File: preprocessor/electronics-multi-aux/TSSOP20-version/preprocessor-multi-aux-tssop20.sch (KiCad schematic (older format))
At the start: 16 parts, among them P1 ST-IN, P2 ST-OUT, P3 TH-IN, P4 TH-OUT, P5 AUX-IN, P6 LIGHT CONTROLLER, P7 AUX2-IN, P8 AUX3-IN, U1 MCP1703T-3302E/CB, U2 LPC812M101JTB16_XSON16

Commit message: Add TSSOP 20 versions
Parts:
- removed R1, R2: 1K, Resistor_SMD:R_0603_1608Metric_Pad1.05x0.95mm_HandSolder, symbol Device:R
- added RN2: R_Pack04, Resistor_SMD:R_Array_Convex_4x0603, symbol Device:R_Pack04
- U2: value LPC812M101JTB16_XSON16 -> LPC812M101JDH20; footprint Package_SON:NXP_XSON-16 -> Package_SO:TSSOP-20_4.4x6.5mm_P0.65mm; symbol MCU_NXP_LPC:LPC812M101JTB16 -> MCU_NXP_LPC:LPC812M101JDH20
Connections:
- wire segments 85 -> 82
- no-connect marks 8 -> 16
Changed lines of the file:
@@
 $EndDescr
 $Comp
-L MCU_NXP_LPC:LPC812M101JTB16 U2
+L MCU_NXP_LPC:LPC812M101JDH20 U2
 U 1 1 58AF9BA8
 P 4850 2550
 F 0 "U2" H 4750 2650 10  0001 C CNN
-F 1 "LPC812M101JTB16_XSON16" H 5550 3100 60  0000 C CNN
-F 2 "Package_SON:NXP_XSON-16" H 4750 2650 60  0001 C CNN
+F 1 "LPC812M101JDH20" H 5550 3200 60  0000 C CNN
+F 2 "Package_SO:TSSOP-20_4.4x6.5mm_P0.65mm" H 4750 2650 60  0001 C CNN
 F 3 "" H 4750 2650 60  0000 C CNN
 	1    4850 2550
@@
 L power:+3V3 #PWR04
 U 1 1 58AFA135
-P 4850 1850
-F 0 "#PWR04" H 4850 1700 50  0001 C CNN
-F 1 "+3V3" H 4850 1990 50  0000 C CNN
-F 2 "" H 4850 1850 50  0000 C CNN
-F 3 "" H 4850 1850 50  0000 C CNN
-	1    4850 1850
+P 4850 1750
+F 0 "#PWR04" H 4850 1600 50  0001 C CNN
+F 1 "+3V3" H 4850 1890 50  0000 C CNN
+F 2 "" H 4850 1750 50  0000 C CNN
+F 3 "" H 4850 1750 50  0000 C CNN
+	1    4850 1750
 	1    0    0    -1
 $EndComp
@@
 Connection ~ 9800 4100
 Wire Wire Line
-	4850 1850 4850 1950
-Wire Wire Line
 	2100 1900 1850 1900
 Wire Wire Line
@@
 	1850 1800 2450 1800
 Wire Wire Line
-	3050 1800 3050 2250
-Wire Wire Line
 	1850 2800 2450 2800
 Wire Wire Line
-	3050 2800 3050 2650
-Wire Wire Line
 	7200 2750 8000 2750
-NoConn ~ 5550 2450
 NoConn ~ 5550 2250
 NoConn ~ 4150 2350
 NoConn ~ 4150 2450
-NoConn ~ 4150 2550
 NoConn ~ 4150 2750
 NoConn ~ 4150 2850
@@
 	2400 1350 2100 1350
 Connection ~ 2100 1350
-Text Label 2650 3750 0    50   ~ 0
+Text Label 2900 3750 2    50   ~ 0
 AUX_IN
-Text Label 2650 2800 0    50   ~ 0
+Text Label 2900 2800 2    50   ~ 0
 TH_IN
-Text Label 2650 1800 0    50   ~ 0
+Text Label 2900 1800 2    50   ~ 0
 ST_IN
 Text Label 7200 2750 0    50   ~ 0
 LIGHT_OUT
-$Comp
-L Device:R R1
-U 1 1 58C77CC2
-P 3300 2250
-F 0 "R1" V 3380 2250 50  0000 C CNN
-F 1 "1K" V 3300 2250 50  0000 C CNN
-F 2 "Resistor_SMD:R_0603_1608Metric_Pad1.05x0.95mm_HandSolder" V 3230 2250 50  0001 C CNN
-F 3 "" H 3300 2250 50  0001 C CNN
-	1    3300 2250
-	0    1    1    0
-$EndComp
-$Comp
-L Device:R R2
-U 1 1 58C77D77
-P 3300 2650
-F 0 "R2" V 3380 2650 50  0000 C CNN
-F 1 "1K" V 3300 2650 50  0000 C CNN
-F 2 "Resistor_SMD:R_0603_1608Metric_Pad1.05x0.95mm_HandSolder" V 3230 2650 50  0001 C CNN
-F 3 "" H 3300 2650 50  0001 C CNN
-	1    3300 2650
-	0    1    1    0
-$EndComp
-Wire Wire Line
-	3050 2250 3150 2250
-Wire Wire Line
-	3050 2650 3150 2650
 $Comp
 L power:PWR_FLAG #FLG013
@@
 	1950 2500 1950 3000
 Wire Wire Line
-	2450 1800 3050 1800
-Wire Wire Line
-	2450 2800 3050 2800
+	2450 1800 2900 1800
+Wire Wire Line
+	2450 2800 2900 2800
 Wire Wire Line
 	2100 1350 2100 1900
@@
 Wire Wire Line
 	1950 4450 1850 4450
-Text Label 2650 4250 0    50   ~ 0
-AUX2_IN
 Connection ~ 2100 3850
 $Comp
@@
 	1950 4950 1850 4950
 Connection ~ 1950 4950
-Text Label 2650 4750 0    50   ~ 0
+Text Label 2900 4750 2    50   ~ 0
 AUX3_IN
 Wire Wire Line
@@
 	8900 4400 8900 4600
 Wire Wire Line
-	4850 3150 4850 3300
-Wire Wire Line
-	3450 2650 4150 2650
-Wire Wire Line
-	6250 2350 5550 2350
-NoConn ~ 5550 2550
-Wire Wire Line
-	5550 2650 5950 2650
-Wire Wire Line
-	3450 2250 4150 2250
-Text Label 6250 2750 2    50   ~ 0
+	4850 3250 4850 3300
+Wire Wire Line
+	3600 2550 4150 2550
+Wire Wire Line
+	6250 2350 5950 2350
+Wire Wire Line
+	3600 2150 4150 2150
+Text Label 6250 2450 2    50   ~ 0
 LIGHT
-Text Label 3600 2250 0    50   ~ 0
+Text Label 3600 2150 0    50   ~ 0
 ST
-Text Label 3600 2650 0    50   ~ 0
+Text Label 3600 2550 0    50   ~ 0
 TH
-Text Label 6250 2850 2    50   ~ 0
+Text Label 6250 2550 2    50   ~ 0
 AUX
+Text Label 3600 2950 0    50   ~ 0
+AUX2
 Text Label 6250 2350 2    50   ~ 0
-AUX2
-Text Label 6250 2650 2    50   ~ 0
 AUX3
 $Comp
@@
 $EndComp
 Wire Wire Line
-	5950 2650 6250 2650
-Connection ~ 5950 2650
-Wire Wire Line
-	5550 2750 6250 2750
-Wire Wire Line
-	5950 2650 5950 2950
-Wire Wire Line
-	5550 2850 6250 2850
-Wire Wire Line
-	3650 3750 3650 4050
-Wire Wire Line
-	3650 4050 4550 4050
-Wire Wire Line
-	1850 3750 3650 3750
-Wire Wire Line
-	3650 4250 3650 4150
-Wire Wire Line
-	3650 4150 4550 4150
-Wire Wire Line
-	1850 4250 3650 4250
-Wire Wire Line
-	3750 4250 3750 4750
-Wire Wire Line
-	1850 4750 3750 4750
-Wire Wire Line
-	3750 4250 4550 4250
+	4000 4050 4550 4050
+Wire Wire Line
+	1850 3750 2900 3750
+Wire Wire Line
+	4000 4150 4550 4150
+Wire Wire Line
+	1850 4750 2900 4750
+Wire Wire Line
+	4000 4250 4550 4250
 Wire Wire Line
 	4550 4350 4000 4350
@@
 Text Label 5500 4250 2    50   ~ 0
 AUX3
+NoConn ~ 4150 2250
+NoConn ~ 4150 2650
+Wire Wire Line
+	4150 2950 3600 2950
+NoConn ~ 5550 2150
+Connection ~ 5950 2350
+Wire Wire Line
+	5950 2350 5550 2350
+Wire Wire Line
+	5950 2350 5950 2950
+Wire Wire Line
+	5550 2450 6250 2450
+Wire Wire Line
+	5550 2550 6250 2550
+NoConn ~ 5550 2650
+NoConn ~ 5550 2750
+NoConn ~ 5550 2950
+NoConn ~ 5550 2850
+$Comp
+L Device:R_Pack04 RN2
+U 1 1 6028CA7F
+P 4750 5000
+F 0 "RN2" V 4333 5000 50  0000 C CNN
+F 1 "R_Pack04" V 4424 5000 50  0000 C CNN
+F 2 "Resistor_SMD:R_Array_Convex_4x0603" V 5025 5000 50  0001 C CNN
+F 3 "~" H 4750 5000 50  0001 C CNN
+	1    4750 5000
+	0    1    1    0
+$EndComp
+Text Label 4000 4050 0    50   ~ 0
+AUX_IN
+Wire Wire Line
+	1850 4250 2900 4250
+Text Label 2900 4250 2    50   ~ 0
+AUX2_IN
+Text Label 4000 4150 0    50   ~ 0
+AUX2_IN
+Text Label 4000 4250 0    50   ~ 0
+AUX3_IN
+Wire Wire Line
+	4000 5000 4550 5000
+Wire Wire Line
+	4000 5100 4550 5100
+NoConn ~ 4550 4900
+NoConn ~ 4550 4800
+NoConn ~ 4950 4900
+NoConn ~ 4950 4800
+Wire Wire Line
+	5500 5000 4950 5000
+Wire Wire Line
+	5500 5100 4950 5100
+Text Label 4000 5000 0    50   ~ 0
+ST_IN
+Text Label 4000 5100 0    50   ~ 0
+TH_IN
+Text Label 5500 5000 2    50   ~ 0
+ST
+Text Label 5500 5100 2    50   ~ 0
+TH
+Wire Wire Line
+	4850 1750 4850 1850
 $EndSCHEMATC

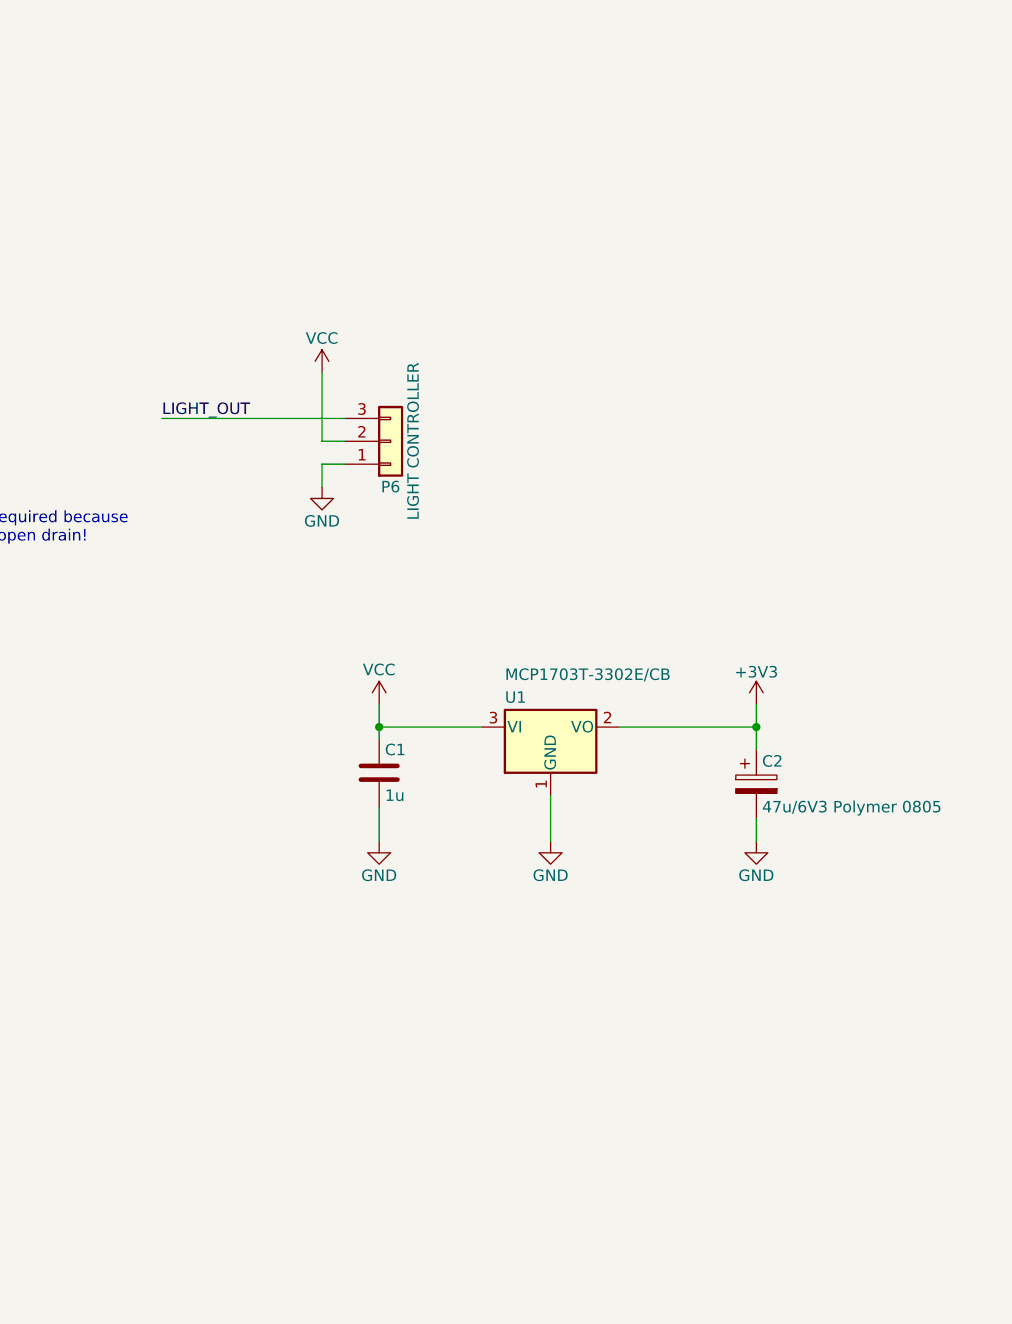
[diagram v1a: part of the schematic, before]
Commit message: Add AUX2 pin assignment info
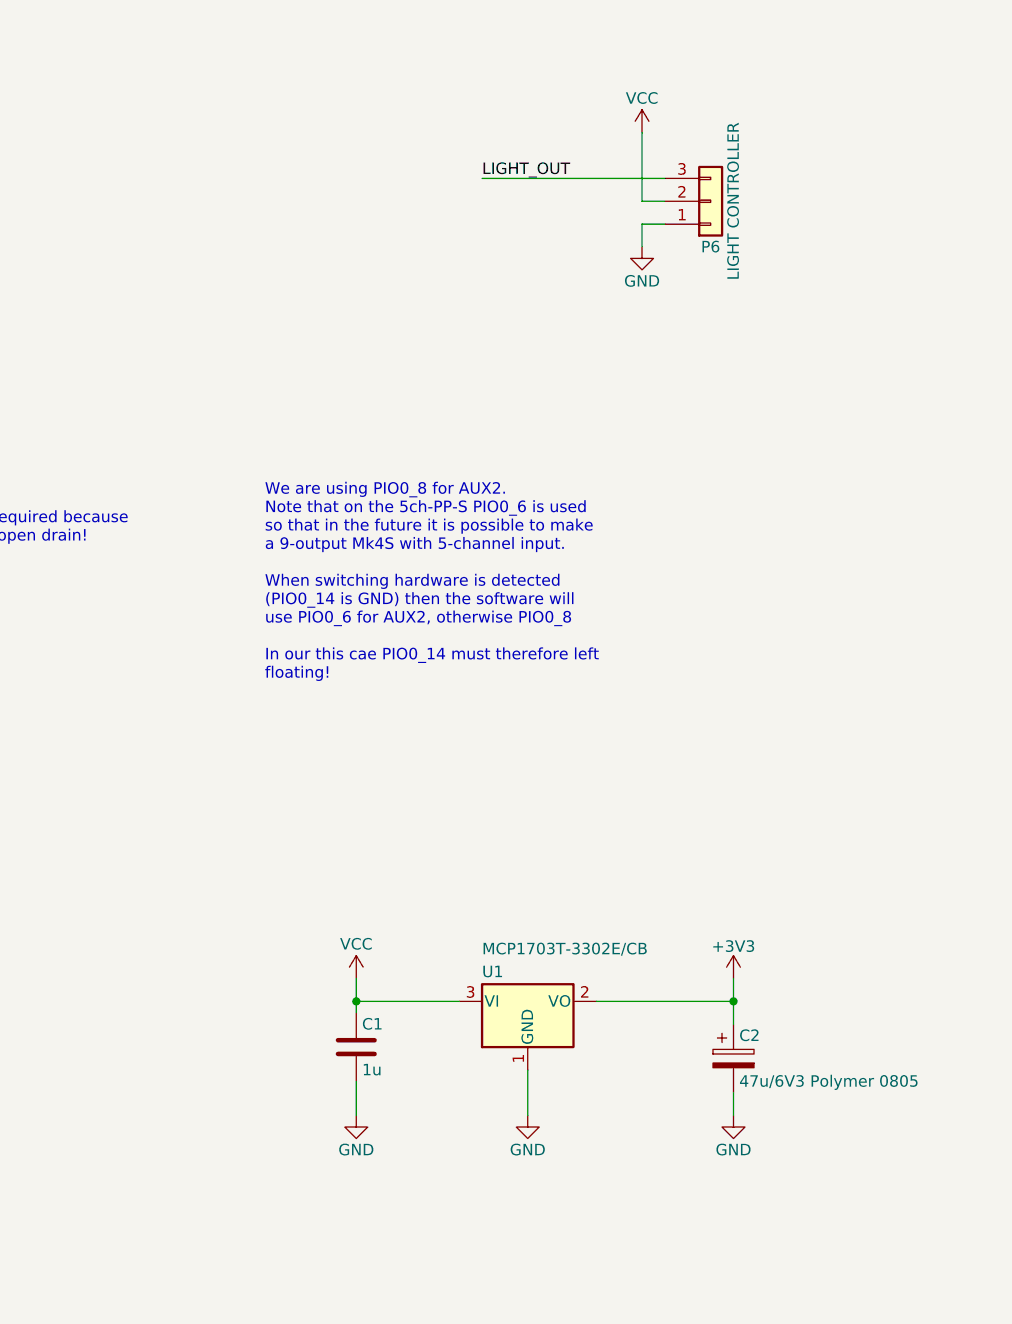
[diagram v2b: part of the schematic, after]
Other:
- note added: "We are using PIO0_8 for AUX2.\nNote that on the 5ch-PP-S PIO0_6 is used\nso that in the future it is possible to make\na 9-output Mk4S with 5-channel input.\n\nWhen switching hardware is detected \n(PIO0_14 is GND) then the software will\nuse PIO0_6 for AUX2, otherwise PIO0_8\n\nIn our this cae PIO0_14 must therefore left \nfloating!"
- moved on the sheet: C1, C2, P6, U1
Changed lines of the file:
@@
 L Regulator_Linear:MCP1703A-3302_SOT23 U1
 U 1 1 58AF9BBC
-P 8900 4100
-F 0 "U1" H 8700 4200 50  0000 L BNN
-F 1 "MCP1703T-3302E/CB" H 8700 4300 50  0000 L BNN
-F 2 "Package_TO_SOT_SMD:SOT-23W" H 9050 3650 30  0001 C CNN
-F 3 "" H 8900 4100 60  0000 C CNN
-	1    8900 4100
+P 8800 5300
+F 0 "U1" H 8600 5400 50  0000 L BNN
+F 1 "MCP1703T-3302E/CB" H 8600 5500 50  0000 L BNN
+F 2 "Package_TO_SOT_SMD:SOT-23W" H 8950 4850 30  0001 C CNN
+F 3 "" H 8800 5300 60  0000 C CNN
+	1    8800 5300
 	1    0    0    -1
 $EndComp
@@
 L Connector_Generic:Conn_01x03 P6
 U 1 1 58AF9DBB
-P 8200 2850
-F 0 "P6" H 8200 3050 50  0000 C CNN
-F 1 "LIGHT CONTROLLER" V 8300 2850 50  0000 C CNN
-F 2 "Connector_PinHeader_2.54mm:PinHeader_1x03_P2.54mm_Vertical" H 8200 2850 50  0001 C CNN
-F 3 "" H 8200 2850 50  0000 C CNN
-	1    8200 2850
+P 9600 1800
+F 0 "P6" H 9600 2000 50  0000 C CNN
+F 1 "LIGHT CONTROLLER" V 9700 1800 50  0000 C CNN
+F 2 "Connector_PinHeader_2.54mm:PinHeader_1x03_P2.54mm_Vertical" H 9600 1800 50  0001 C CNN
+F 3 "" H 9600 1800 50  0000 C CNN
+	1    9600 1800
 	1    0    0    1
 $EndComp
@@
 L power:GND #PWR02
 U 1 1 58AFA0BE
-P 8150 4600
-F 0 "#PWR02" H 8150 4350 50  0001 C CNN
-F 1 "GND" H 8150 4450 50  0000 C CNN
-F 2 "" H 8150 4600 50  0000 C CNN
-F 3 "" H 8150 4600 50  0000 C CNN
-	1    8150 4600
+P 8050 5800
+F 0 "#PWR02" H 8050 5550 50  0001 C CNN
+F 1 "GND" H 8050 5650 50  0000 C CNN
+F 2 "" H 8050 5800 50  0000 C CNN
+F 3 "" H 8050 5800 50  0000 C CNN
+	1    8050 5800
 	1    0    0    -1
 $EndComp
@@
 L power:VCC #PWR06
 U 1 1 58AFA193
-P 8150 4000
-F 0 "#PWR06" H 8150 3850 50  0001 C CNN
-F 1 "VCC" H 8150 4150 50  0000 C CNN
-F 2 "" H 8150 4000 50  0000 C CNN
-F 3 "" H 8150 4000 50  0000 C CNN
-	1    8150 4000
+P 8050 5200
+F 0 "#PWR06" H 8050 5050 50  0001 C CNN
+F 1 "VCC" H 8050 5350 50  0000 C CNN
+F 2 "" H 8050 5200 50  0000 C CNN
+F 3 "" H 8050 5200 50  0000 C CNN
+	1    8050 5200
 	1    0    0    -1
 $EndComp
@@
 L Device:C C1
 U 1 1 58AFA243
-P 8150 4300
-F 0 "C1" H 8175 4400 50  0000 L CNN
-F 1 "1u" H 8175 4200 50  0000 L CNN
-F 2 "Capacitor_SMD:C_0805_2012Metric_Pad1.15x1.40mm_HandSolder" H 8188 4150 50  0001 C CNN
-F 3 "" H 8150 4300 50  0000 C CNN
-	1    8150 4300
+P 8050 5500
+F 0 "C1" H 8075 5600 50  0000 L CNN
+F 1 "1u" H 8075 5400 50  0000 L CNN
+F 2 "Capacitor_SMD:C_0805_2012Metric_Pad1.15x1.40mm_HandSolder" H 8088 5350 50  0001 C CNN
+F 3 "" H 8050 5500 50  0000 C CNN
+	1    8050 5500
 	1    0    0    -1
 $EndComp
@@
 L power:GND #PWR07
 U 1 1 58AFA4AA
-P 8900 4600
-F 0 "#PWR07" H 8900 4350 50  0001 C CNN
-F 1 "GND" H 8900 4450 50  0000 C CNN
-F 2 "" H 8900 4600 50  0000 C CNN
-F 3 "" H 8900 4600 50  0000 C CNN
-	1    8900 4600
-	1    0    0    -1
-$EndComp
-Wire Wire Line
-	8150 4000 8150 4100
-Wire Wire Line
-	8150 4450 8150 4600
-Connection ~ 8150 4100
+P 8800 5800
+F 0 "#PWR07" H 8800 5550 50  0001 C CNN
+F 1 "GND" H 8800 5650 50  0000 C CNN
+F 2 "" H 8800 5800 50  0000 C CNN
+F 3 "" H 8800 5800 50  0000 C CNN
+	1    8800 5800
+	1    0    0    -1
+$EndComp
+Wire Wire Line
+	8050 5200 8050 5300
+Wire Wire Line
+	8050 5650 8050 5800
+Connection ~ 8050 5300
 $Comp
 L Device:CP C2
 U 1 1 58AFA5B0
-P 9800 4350
-F 0 "C2" H 9825 4450 50  0000 L CNN
-F 1 "47u/6V3 Polymer 0805" H 9825 4250 50  0000 L CNN
-F 2 "Capacitor_SMD:C_0805_2012Metric_Pad1.15x1.40mm_HandSolder" H 9838 4200 50  0001 C CNN
-F 3 "" H 9800 4350 50  0000 C CNN
-	1    9800 4350
+P 9700 5550
+F 0 "C2" H 9725 5650 50  0000 L CNN
+F 1 "47u/6V3 Polymer 0805" H 9725 5450 50  0000 L CNN
+F 2 "Capacitor_SMD:C_0805_2012Metric_Pad1.15x1.40mm_HandSolder" H 9738 5400 50  0001 C CNN
+F 3 "" H 9700 5550 50  0000 C CNN
+	1    9700 5550
 	1    0    0    -1
 $EndComp
@@
 L power:+3V3 #PWR08
 U 1 1 58AFA5F4
-P 9800 4000
-F 0 "#PWR08" H 9800 3850 50  0001 C CNN
-F 1 "+3V3" H 9800 4140 50  0000 C CNN
-F 2 "" H 9800 4000 50  0000 C CNN
-F 3 "" H 9800 4000 50  0000 C CNN
-	1    9800 4000
+P 9700 5200
+F 0 "#PWR08" H 9700 5050 50  0001 C CNN
+F 1 "+3V3" H 9700 5340 50  0000 C CNN
+F 2 "" H 9700 5200 50  0000 C CNN
+F 3 "" H 9700 5200 50  0000 C CNN
+	1    9700 5200
 	1    0    0    -1
 $EndComp
@@
 L power:GND #PWR09
 U 1 1 58AFA6CA
-P 9800 4600
-F 0 "#PWR09" H 9800 4350 50  0001 C CNN
-F 1 "GND" H 9800 4450 50  0000 C CNN
-F 2 "" H 9800 4600 50  0000 C CNN
-F 3 "" H 9800 4600 50  0000 C CNN
-	1    9800 4600
-	1    0    0    -1
-$EndComp
-Wire Wire Line
-	9800 4500 9800 4600
-Wire Wire Line
-	9800 4000 9800 4100
-Connection ~ 9800 4100
+P 9700 5800
+F 0 "#PWR09" H 9700 5550 50  0001 C CNN
+F 1 "GND" H 9700 5650 50  0000 C CNN
+F 2 "" H 9700 5800 50  0000 C CNN
+F 3 "" H 9700 5800 50  0000 C CNN
+	1    9700 5800
+	1    0    0    -1
+$EndComp
+Wire Wire Line
+	9700 5700 9700 5800
+Wire Wire Line
+	9700 5200 9700 5300
+Connection ~ 9700 5300
 Wire Wire Line
 	2100 1900 1850 1900
@@
 L power:VCC #PWR010
 U 1 1 58AFAD17
-P 7900 2550
-F 0 "#PWR010" H 7900 2400 50  0001 C CNN
-F 1 "VCC" H 7900 2700 50  0000 C CNN
-F 2 "" H 7900 2550 50  0000 C CNN
-F 3 "" H 7900 2550 50  0000 C CNN
-	1    7900 2550
+P 9300 1500
+F 0 "#PWR010" H 9300 1350 50  0001 C CNN
+F 1 "VCC" H 9300 1650 50  0000 C CNN
+F 2 "" H 9300 1500 50  0000 C CNN
+F 3 "" H 9300 1500 50  0000 C CNN
+	1    9300 1500
 	1    0    0    -1
 $EndComp
@@
 L power:GND #PWR011
 U 1 1 58AFADBD
-P 7900 3050
-F 0 "#PWR011" H 7900 2800 50  0001 C CNN
-F 1 "GND" H 7900 2900 50  0000 C CNN
-F 2 "" H 7900 3050 50  0000 C CNN
-F 3 "" H 7900 3050 50  0000 C CNN
-	1    7900 3050
-	1    0    0    -1
-$EndComp
-Wire Wire Line
-	8000 2850 7900 2850
-Wire Wire Line
-	7900 2850 7900 2550
-Wire Wire Line
-	8000 2950 7900 2950
-Wire Wire Line
-	7900 2950 7900 3050
+P 9300 2000
+F 0 "#PWR011" H 9300 1750 50  0001 C CNN
+F 1 "GND" H 9300 1850 50  0000 C CNN
+F 2 "" H 9300 2000 50  0000 C CNN
+F 3 "" H 9300 2000 50  0000 C CNN
+	1    9300 2000
+	1    0    0    -1
+$EndComp
+Wire Wire Line
+	9400 1800 9300 1800
+Wire Wire Line
+	9300 1800 9300 1500
+Wire Wire Line
+	9400 1900 9300 1900
+Wire Wire Line
+	9300 1900 9300 2000
 Wire Wire Line
 	1850 1800 2450 1800
@@
 	1850 2800 2450 2800
 Wire Wire Line
-	7200 2750 8000 2750
+	8600 1700 9400 1700
 NoConn ~ 5550 2250
 NoConn ~ 4150 2350
@@
 Text Label 2900 1800 2    50   ~ 0
 ST_IN
-Text Label 7200 2750 0    50   ~ 0
+Text Label 8600 1700 0    50   ~ 0
 LIGHT_OUT
 $Comp
@@
 Connection ~ 1950 5500
 Wire Wire Line
-	8150 4100 8150 4150
-Wire Wire Line
-	9800 4100 9800 4200
+	8050 5300 8050 5350
+Wire Wire Line
+	9700 5300 9700 5400
 Wire Wire Line
 	2100 1900 2100 2400
@@
 Pull-down required because \nPIO0_11 is open drain!
 Wire Wire Line
-	9200 4100 9800 4100
-Wire Wire Line
-	8150 4100 8600 4100
-Wire Wire Line
-	8900 4400 8900 4600
+	9100 5300 9700 5300
+Wire Wire Line
+	8050 5300 8500 5300
+Wire Wire Line
+	8800 5600 8800 5800
 Wire Wire Line
 	4850 3250 4850 3300
@@
 Wire Wire Line
 	4850 1750 4850 1850
+Text Notes 7650 3900 0    50   ~ 0
+We are using PIO0_8 for AUX2.\nNote that on the 5ch-PP-S PIO0_6 is used\nso that in the future it is possible to make\na 9-output Mk4S with 5-channel input.\n\nWhen switching hardware is detected \n(PIO0_14 is GND) then the software will\nuse PIO0_6 for AUX2, otherwise PIO0_8\n\nIn our this cae PIO0_14 must therefore left \nfloating!
 $EndSCHEMATC
